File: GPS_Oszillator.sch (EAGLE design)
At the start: 34 parts, among them IC1 74ACT04D, IC2 7805TV, X1 ST-SMB-V, X2 ST-SMB-V

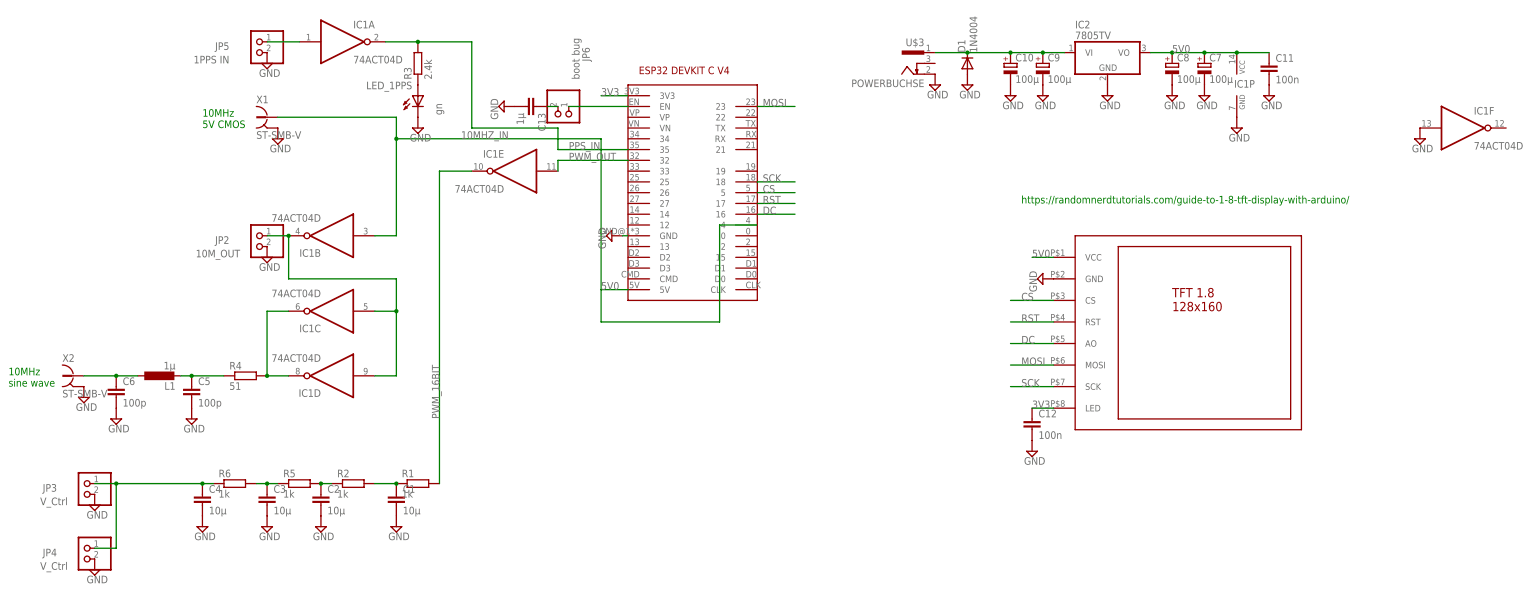
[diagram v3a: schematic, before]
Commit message: add second power connector and sort out drc errors
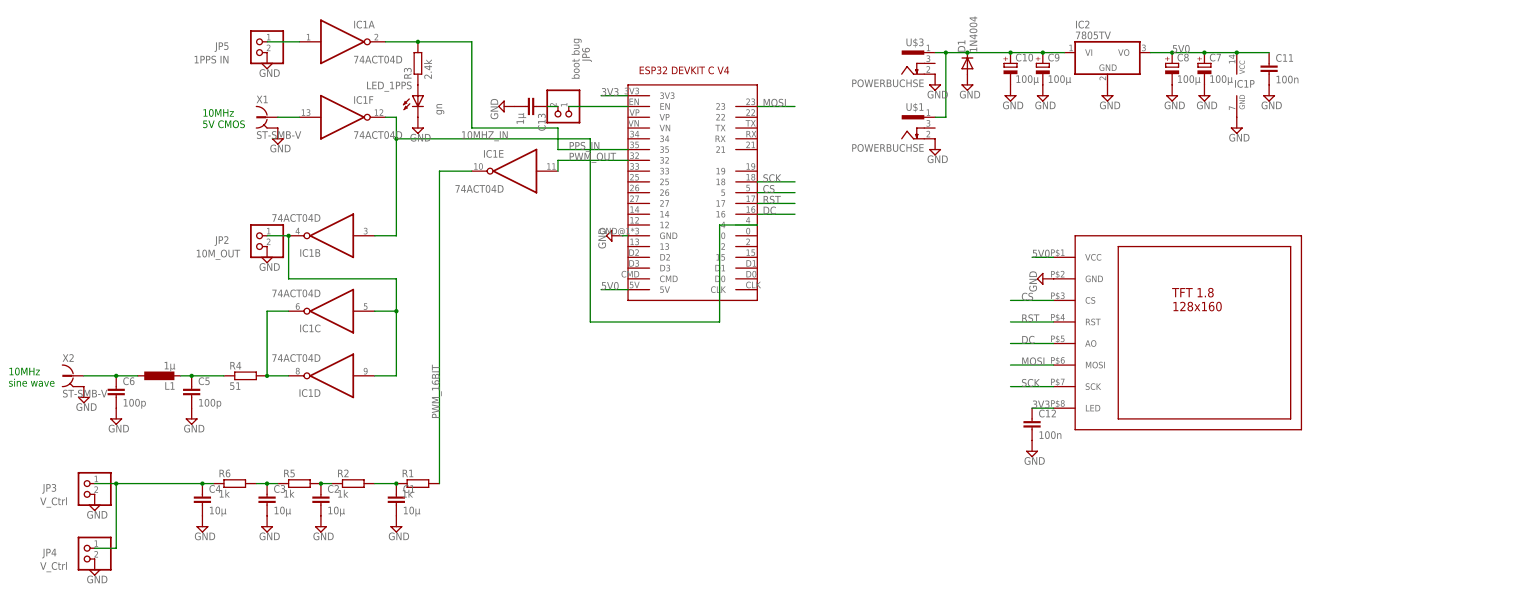
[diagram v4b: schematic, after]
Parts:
- added U$1: POWERBUCHSE, _Winni:POWERBUCHSE
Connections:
- new net N$13: IC1F.I, X1.1
- net 10MHZ_IN: now also IC1F.O; no longer X1.1
- net GND: now also U$1.2; no longer IC1F.I
- net N$12: now also U$1.1
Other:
- note removed: "https://randomnerdtutorials.com/guide-to-1-8-tft-display-with-arduino/"
- moved on the sheet: IC1F
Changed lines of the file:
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@@
 <setting verticaltext="up"/>
 </settings>
-<grid distance="25" unitdist="mil" unit="mil" style="lines" multiple="1" display="no" altdistance="0.01" altunitdist="inch" altunit="inch"/>
+<grid distance="0.1" unitdist="inch" unit="inch" style="lines" multiple="1" display="no" altdistance="0.01" altunitdist="inch" altunit="inch"/>
 <layers>
 <layer number="1" name="Top" color="4" fill="1" visible="no" active="no"/>
@@
 <part name="U$3" library="_Winni" deviceset="POWERBUCHSE" device=""/>
 <part name="SUPPLY26" library="supply2" deviceset="GND" device=""/>
-<part name="SUPPLY25" library="supply2" deviceset="GND" device=""/>
 <part name="D1" library="diode" deviceset="1N4004" device=""/>
 <part name="SUPPLY28" library="supply2" deviceset="GND" device=""/>
@@
 <part name="SUPPLY3" library="supply2" deviceset="GND" device=""/>
 <part name="SUPPLY7" library="supply2" deviceset="GND" device=""/>
+<part name="U$1" library="_Winni" deviceset="POWERBUCHSE" device=""/>
+<part name="SUPPLY8" library="supply2" deviceset="GND" device=""/>
 </parts>
 <sheets>
@@
 <text x="-144.78" y="15.24" size="1.778" layer="91">10MHz
 sine wave</text>
-<text x="93.98" y="58.42" size="1.778" layer="91">https://randomnerdtutorials.com/guide-to-1-8-tft-display-with-arduino/</text>
 </plain>
 <instances>
@@
 <instance part="IC1" gate="D" x="-68.58" y="17.78" rot="R180"/>
 <instance part="IC1" gate="E" x="-25.4" y="66.04" rot="MR0"/>
-<instance part="IC1" gate="F" x="198.12" y="76.2"/>
+<instance part="IC1" gate="F" x="-66.04" y="78.74"/>
 <instance part="IC1" gate="P" x="144.78" y="86.36"/>
 <instance part="X1" gate="G1" x="-83.82" y="78.74"/>
@@
 <instance part="U$3" gate="G$1" x="68.58" y="91.44" rot="MR0"/>
 <instance part="SUPPLY26" gate="GND" x="73.66" y="86.36"/>
-<instance part="SUPPLY25" gate="GND" x="187.96" y="73.66"/>
 <instance part="D1" gate="1" x="81.28" y="91.44" rot="R90"/>
 <instance part="SUPPLY28" gate="GND" x="81.28" y="86.36"/>
@@
 <instance part="SUPPLY3" gate="GND" x="-83.82" y="-17.78"/>
 <instance part="SUPPLY7" gate="GND" x="-99.06" y="-17.78"/>
+<instance part="U$1" gate="G$1" x="68.58" y="76.2" rot="MR0"/>
+<instance part="SUPPLY8" gate="GND" x="73.66" y="71.12"/>
 </instances>
 <busses>
@@
 </segment>
 <segment>
-<pinref part="IC1" gate="F" pin="I"/>
-<pinref part="SUPPLY25" gate="GND" pin="GND"/>
-</segment>
-<segment>
 <pinref part="D1" gate="1" pin="A"/>
 <pinref part="SUPPLY28" gate="GND" pin="GND"/>
@@
 <pinref part="C4" gate="G$1" pin="2"/>
 <pinref part="SUPPLY7" gate="GND" pin="GND"/>
+</segment>
+<segment>
+<pinref part="U$1" gate="G$1" pin="2"/>
+<pinref part="SUPPLY8" gate="GND" pin="GND"/>
 </segment>
 </net>
@@
 <net name="10MHZ_IN" class="0">
 <segment>
-<pinref part="X1" gate="G1" pin="1"/>
-<wire x1="-81.28" y1="78.74" x2="-53.34" y2="78.74" width="0.1524" layer="91"/>
+<wire x1="-55.88" y1="78.74" x2="-53.34" y2="78.74" width="0.1524" layer="91"/>
 <wire x1="-53.34" y1="78.74" x2="-53.34" y2="73.66" width="0.1524" layer="91"/>
 <pinref part="IC1" gate="B" pin="I"/>
@@
 <junction x="-53.34" y="73.66"/>
 <label x="-38.1" y="73.66" size="1.778" layer="95"/>
-<wire x1="-5.08" y1="73.66" x2="-53.34" y2="73.66" width="0.1524" layer="91"/>
+<wire x1="-7.62" y1="73.66" x2="-53.34" y2="73.66" width="0.1524" layer="91"/>
 <wire x1="22.86" y1="53.34" x2="22.86" y2="30.48" width="0.1524" layer="91"/>
-<wire x1="22.86" y1="30.48" x2="-5.08" y2="30.48" width="0.1524" layer="91"/>
-<wire x1="-5.08" y1="30.48" x2="-5.08" y2="73.66" width="0.1524" layer="91"/>
+<wire x1="22.86" y1="30.48" x2="-7.62" y2="30.48" width="0.1524" layer="91"/>
+<wire x1="-7.62" y1="30.48" x2="-7.62" y2="73.66" width="0.1524" layer="91"/>
 <wire x1="31.75" y1="53.34" x2="22.86" y2="53.34" width="0.1524" layer="91"/>
 <pinref part="U$4" gate="G$1" pin="4"/>
+<pinref part="IC1" gate="F" pin="O"/>
 </segment>
 </net>
@@
 <pinref part="U$3" gate="G$1" pin="1"/>
 <pinref part="D1" gate="1" pin="C"/>
-<wire x1="81.28" y1="93.98" x2="73.66" y2="93.98" width="0.1524" layer="91"/>
+<wire x1="81.28" y1="93.98" x2="76.2" y2="93.98" width="0.1524" layer="91"/>
 <junction x="81.28" y="93.98"/>
+<pinref part="U$1" gate="G$1" pin="1"/>
+<wire x1="76.2" y1="93.98" x2="73.66" y2="93.98" width="0.1524" layer="91"/>
+<wire x1="73.66" y1="78.74" x2="76.2" y2="78.74" width="0.1524" layer="91"/>
+<wire x1="76.2" y1="78.74" x2="76.2" y2="93.98" width="0.1524" layer="91"/>
+<junction x="76.2" y="93.98"/>
 </segment>
 </net>
@@
 </segment>
 </net>
+<net name="N$13" class="0">
+<segment>
+<pinref part="X1" gate="G1" pin="1"/>
+<wire x1="-81.28" y1="78.74" x2="-76.2" y2="78.74" width="0.1524" layer="91"/>
+<pinref part="IC1" gate="F" pin="I"/>
+</segment>
+</net>

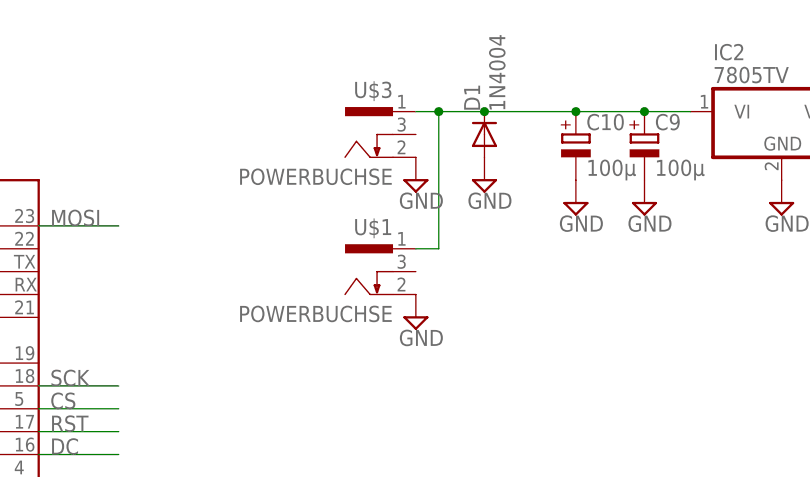
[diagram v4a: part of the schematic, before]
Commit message: Fix reversed DC Jacks
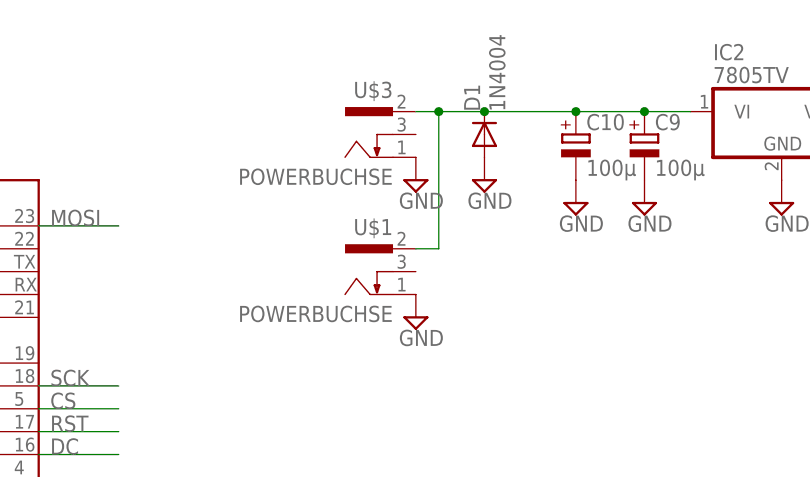
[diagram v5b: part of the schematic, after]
